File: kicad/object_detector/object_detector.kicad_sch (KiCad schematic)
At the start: 0 parts

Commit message: put my sutff on kicad schematic
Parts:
- added C1: 220u, Capacitor_SMD:CP_Elec_8x10, symbol Device:C_Polarized
- added C2: 100n, Capacitor_SMD:C_1206_3216Metric_Pad1.33x1.80mm_HandSolder, symbol Device:C_Small
- added C3: 1u, Capacitor_THT:C_Rect_L7.0mm_W4.5mm_P5.00mm, symbol Device:C_Small
- added C4: 47n, Resistor_SMD:R_0805_2012Metric_Pad1.20x1.40mm_HandSolder, symbol Device:C_Small
- added Display: Conn_01x04, Connector_JST:JST_PH_B4B-PH-K_1x04_P2.00mm_Vertical, symbol Connector_Generic:Conn_01x04
- added R1: 100R, Resistor_SMD:R_1206_3216Metric_Pad1.30x1.75mm_HandSolder, symbol Device:R_Small_US
- added Speaker: Conn_01x02, Connector_JST:JST_PH_B2B-PH-K_1x02_P2.00mm_Vertical, symbol Connector_Generic:Conn_01x02
- added TP1: DAC_signal, symbol Connector:TestPoint_Alt
- added TP2: Spk_signal, symbol Connector:TestPoint_Alt
- added TP3: SCL, symbol Connector:TestPoint_Alt
- added TP4: SDA, symbol Connector:TestPoint_Alt
- added U1: LM386, Package_SO:SOIC-8-1EP_3.9x4.9mm_P1.27mm_EP2.29x3mm, symbol Amplifier_Audio:LM386
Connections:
- new net: C1.1, C3.1, R1.2
- new net: C1.2, Speaker.1 (Pin_1), TP2.1
- new net: C2.1, TP1.1
- new net: C2.2, U1.3 (+)
- new net: C4.2, U1.7 (BYPASS)
- new net: R1.1, U1.5
- new net 5V: Display.1 (Pin_1), U1.6 (V+)
- new net GND: C3.2, C4.1, Display.2 (Pin_2), Speaker.2 (Pin_2), U1.2 (-), U1.4 (GND)
- new net SCL: Display.3 (Pin_3), TP3.1
- new net SDA: Display.4 (Pin_4), TP4.1

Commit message: kicad layout for ramus stuff
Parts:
- added BUTTONS1, SENSOR1: Conn_01x05, Connector_JST:JST_PH_B5B-PH-K_1x05_P2.00mm_Vertical, symbol Connector_Generic:Conn_01x05
- added C5: 100n, Capacitor_SMD:C_1206_3216Metric_Pad1.33x1.80mm_HandSolder, symbol Device:C_Small
- added µC1: ~, RF_Module:ESP32-C3-DevKitM-1, symbol custom_ece342:ESP32_WROOM
- TP1, TP2: footprint (none) -> TestPoint:TestPoint_2Pads_Pitch5.08mm_Drill1.3mm
- TP3, TP4: footprint (none) -> Connector_PinHeader_2.54mm:PinHeader_1x01_P2.54mm_Vertical
- renumbered Display to Display1, Speaker to Speaker1
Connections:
- net 5V: now also C5.2, µC1. (3.3V)
- net GND: now also BUTTONS1.5 (Pin_5), C5.1, SENSOR1.5 (Pin_5), µC1. (3.3V)
- net SCL: now also µC1. (3.3V)
- net SDA: now also µC1. (3.3V)
- net DAC: now reaches C2.1, TP1.1
- net DAC: now also µC1. (3.3V)
- new net BRIGHTNESS: BUTTONS1.2 (Pin_2)
- new net RESET: BUTTONS1.1 (Pin_1), µC1. (3.3V)
- new net TIME_DEC: BUTTONS1.4 (Pin_4)
- new net TIME_INC: BUTTONS1.3 (Pin_3)
- new net WEIGH_1: SENSOR1.1 (Pin_1)
- new net WEIGH_2: SENSOR1.2 (Pin_2)
- new net WEIGH_3: SENSOR1.3 (Pin_3)
- new net WEIGH_4: SENSOR1.4 (Pin_4)
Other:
- note added: "2/20/2026"
- note added: "ECE 342 – Group 01 Nick Gerbavac John Ramus Arthur Roth"
- note added: "Object Detector"

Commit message: updated PCB schematic
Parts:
- removed µC1: ~, RF_Module:ESP32-C3-DevKitM-1, symbol custom_ece342:ESP32_WROOM
- added C6, C7: 10uF, Capacitor_SMD:C_1206_3216Metric, symbol Device:C
- added D1: B220, Diode_SMD:D_SMA, symbol Device:D_Schottky
- added D2: LED, LED_SMD:LED_0603_1608Metric, symbol Device:LED
- added H1, H2, H3, H4: MountingHole, MountingHole:MountingHole_2.2mm_M2, symbol Mechanical:MountingHole
- added J1: Terminal In, TerminalBlock_TE-Connectivity:TerminalBlock_TE_282834-2_1x02_P2.54mm_Horizontal, symbol Connector:Screw_Terminal_01x02
- added R2: 560, Resistor_SMD:R_0805_2012Metric, symbol Device:R
- added U2: ESP32_DevKitC, ESP32:ESP32_DevKitC_38pin_socket, symbol ESP32:ESP32_DevKitC
- added U3: NCP1117-5.0_SOT223, Package_TO_SOT_SMD:SOT-223-3_TabPin2, symbol ncp1117-5.0_sot223:NCP1117-5.0_SOT223
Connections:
- net 5V: now also C7.1, U2.19 (5V_in), U3.2 (VO)
- net BRIGHTNESS: now also U2.31 (IO_19)
- net DAC: now also U2.9 (IO_25)
- net GND: now also C6.2, C7.2, D2.1 (K), J1.1 (Pin_1), U2.14 (GND), U2.32 (GND), U2.38 (GND), U3.1 (GND)
- net RESET: now also U2.2 (EN)
- net SCL: now also U2.36 (IO_22)
- net SDA: now also U2.33 (IO_21)
- net TIME_DEC: now also U2.28 (IO_17)
- net TIME_INC: now also U2.30 (IO_18)
- net WEIGH_1: now also U2.10 (IO_26)
- net WEIGH_2: now also U2.11 (IO_27)
- net WEIGH_3: now also U2.7 (IO_32)
- net WEIGH_4: now also U2.8 (IO_33)
- new net: C6.1, D1.1 (K), R2.1, U3.3 (VI)
- new net: D2.2 (A), R2.2
- new net: D1.2 (A), J1.2 (Pin_2)
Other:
- note added: "5V Power Supply"
- note added: "Alarm and Display"
- note added: "ECE 342 – Group 01 Nicholas Gerbavac John Ramus Arthur Roth"
- note added: "ESP32 DevKitC Module"
- note added: "M2 Screws"
- note added: "Mounting Holes"
- note added: "UI Buttons and Object Sensor output"
- note removed: "ECE 342 – Group 01 Nick Gerbavac John Ramus Arthur Roth"
- moved on the sheet: BUTTONS1, C1, C2, C3, C4, C5, Display1, R1, SENSOR1, Speaker1, TP1, TP2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

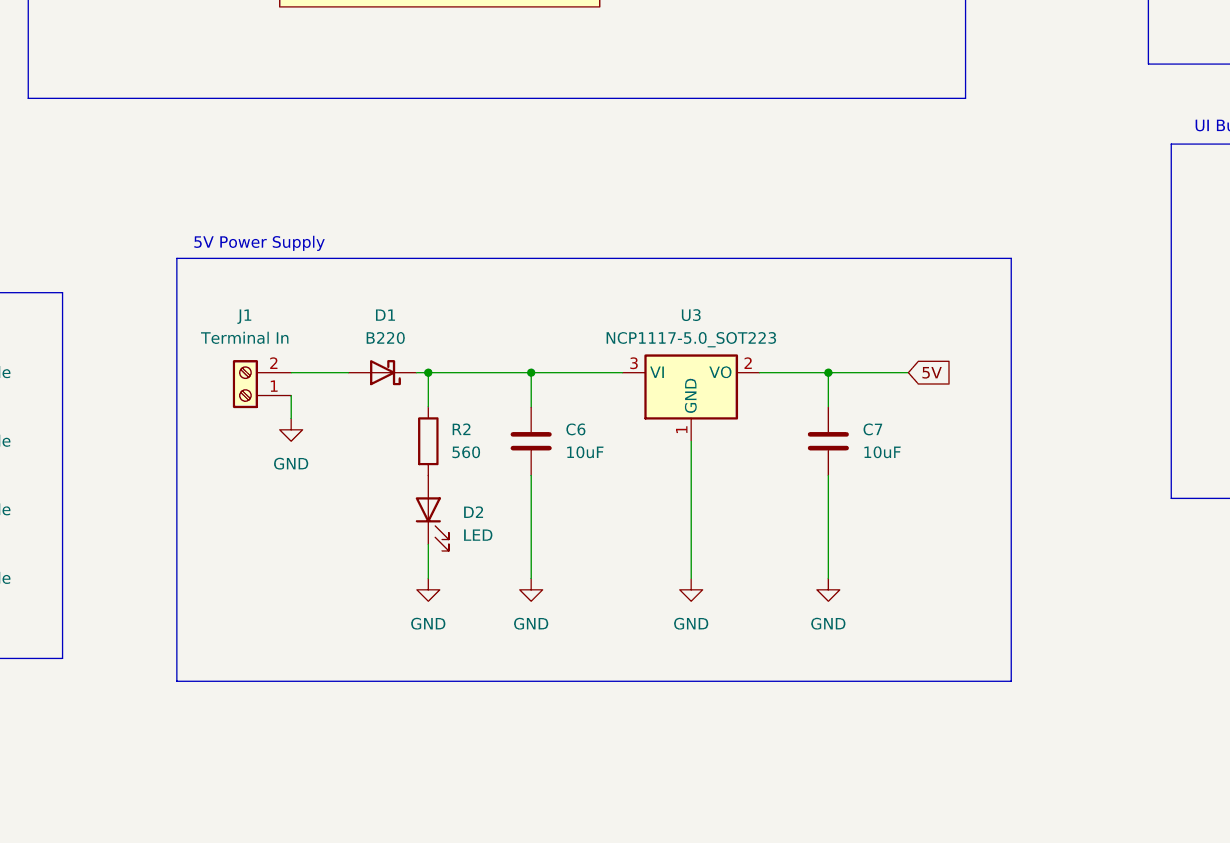
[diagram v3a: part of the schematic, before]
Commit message: changed LDO connector input
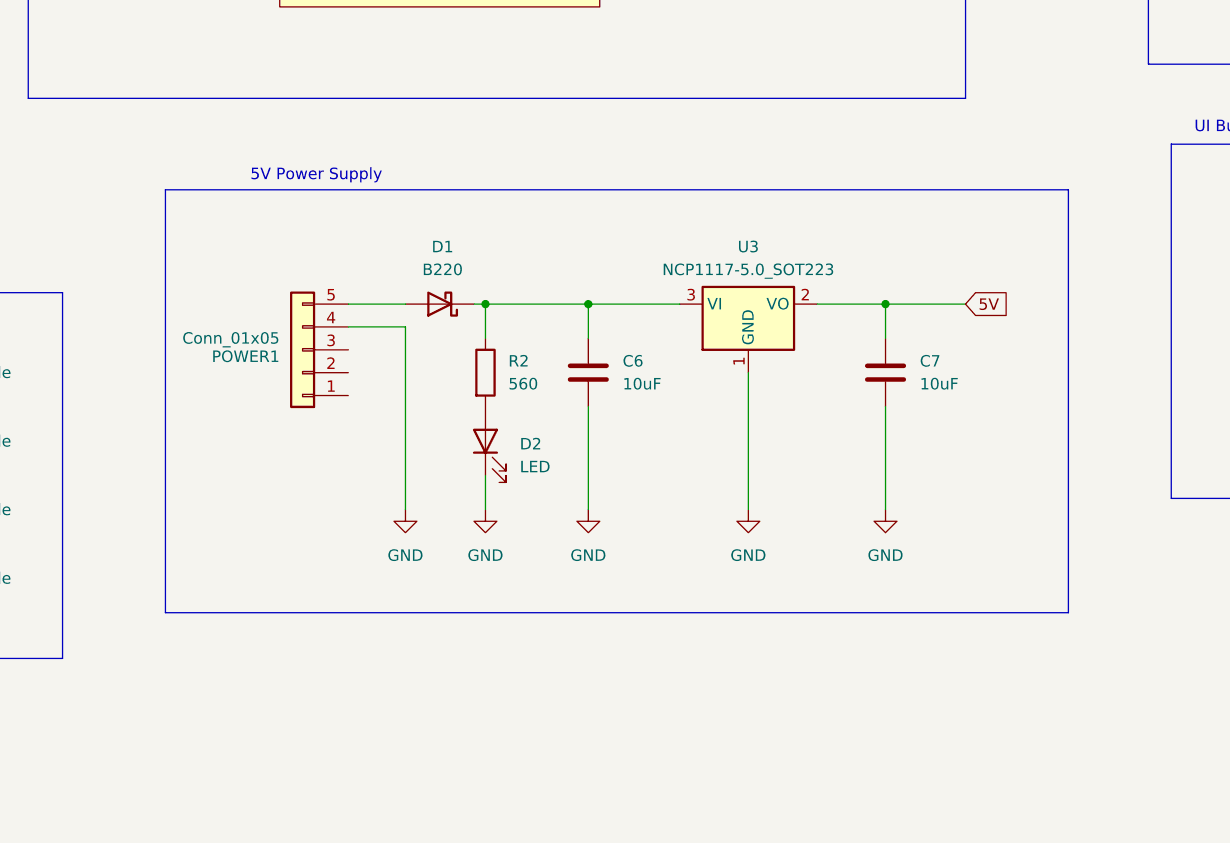
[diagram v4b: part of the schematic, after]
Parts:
- removed J1: Terminal In, TerminalBlock_TE-Connectivity:TerminalBlock_TE_282834-2_1x02_P2.54mm_Horizontal, symbol Connector:Screw_Terminal_01x02
- added POWER1: Conn_01x05, Connector_JST:JST_PH_B5B-PH-K_1x05_P2.00mm_Vertical, symbol Connector_Generic:Conn_01x05
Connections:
- net GND: now also POWER1.4 (Pin_4)
- net at D1.2 (A): now also POWER1.5 (Pin_5)
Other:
- moved on the sheet: C6, C7, D1, D2, R2, U3

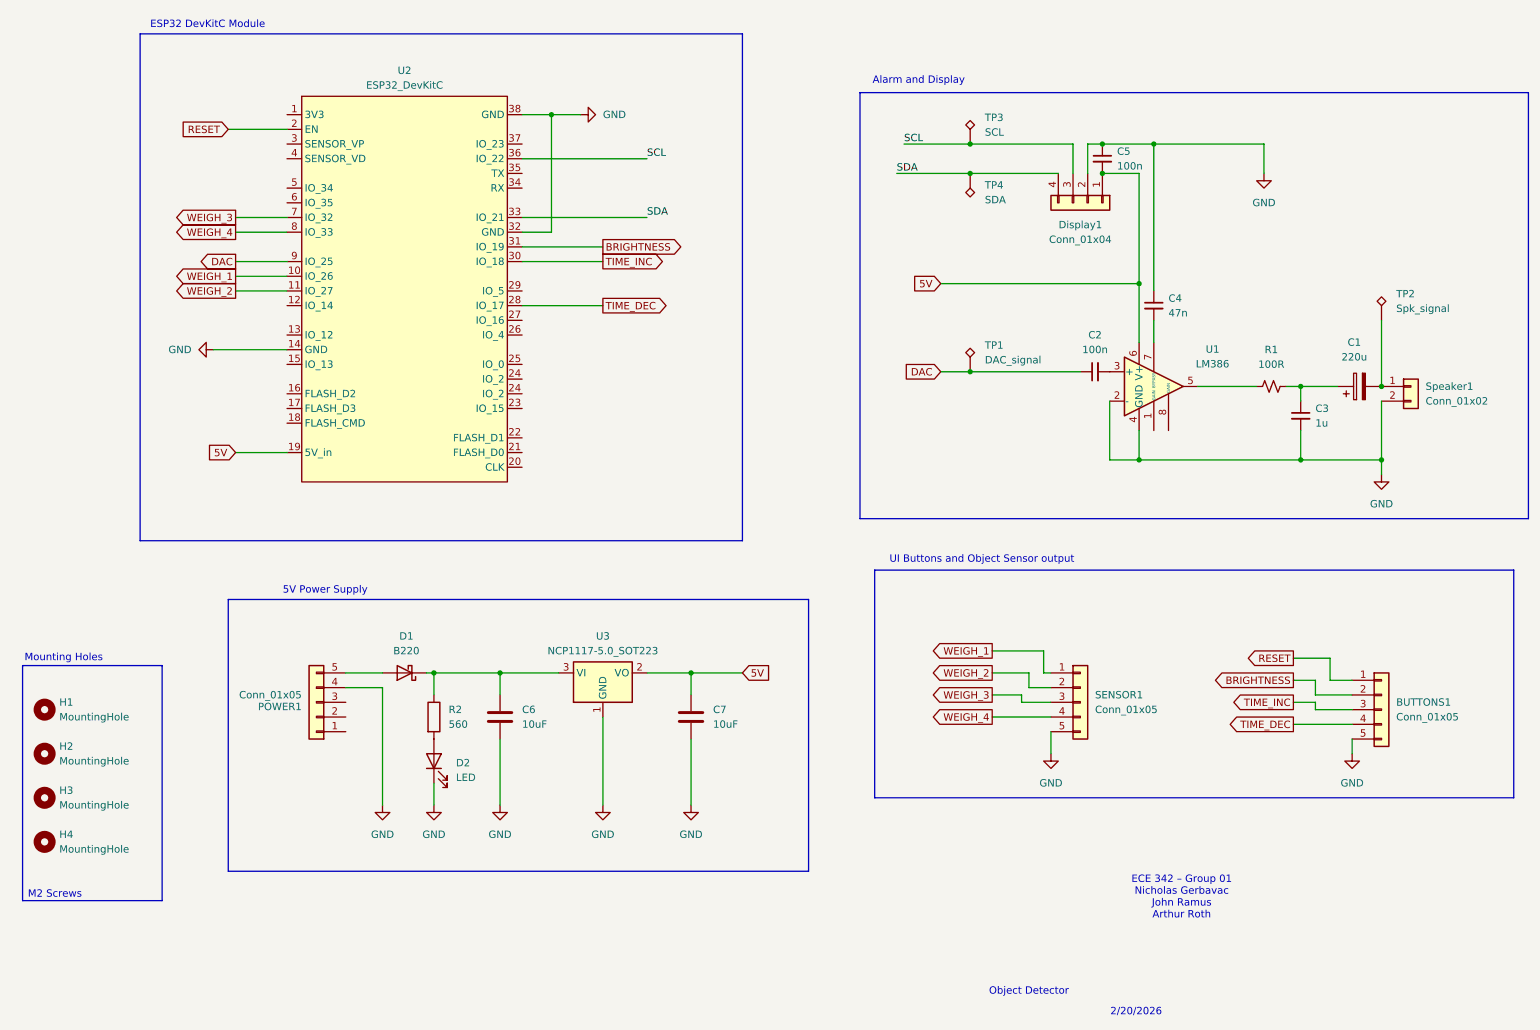
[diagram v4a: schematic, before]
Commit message: preliminary layout
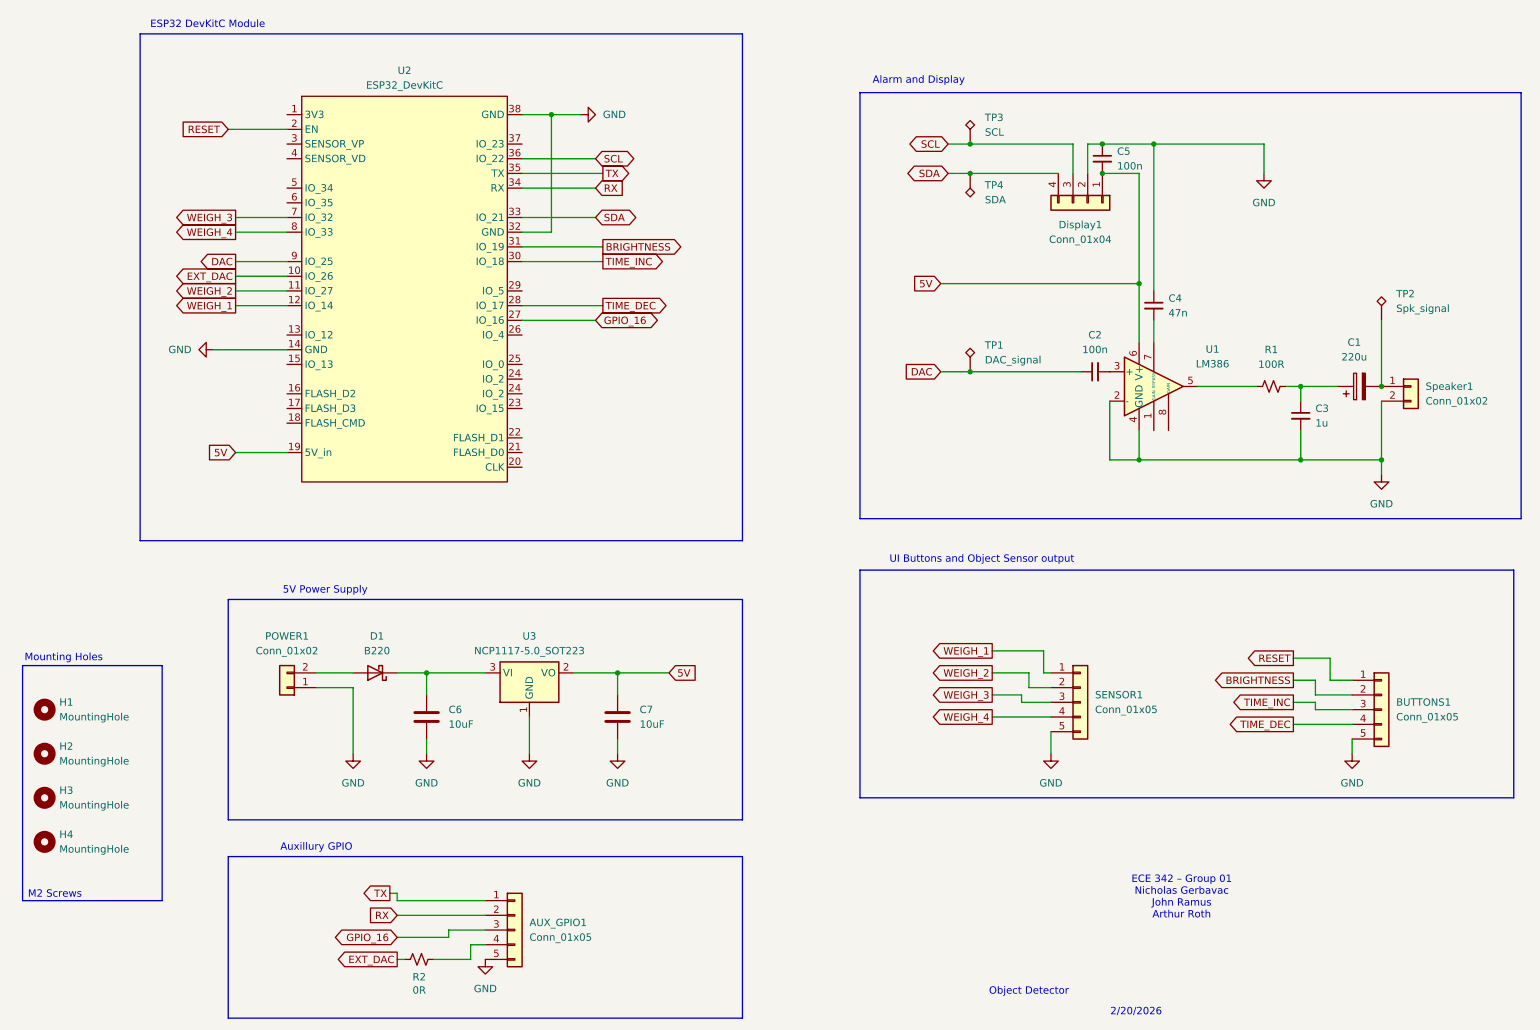
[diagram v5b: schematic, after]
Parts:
- removed D2: LED, LED_SMD:LED_0603_1608Metric, symbol Device:LED
- removed POWER1: Conn_01x05, Connector_JST:JST_PH_B5B-PH-K_1x05_P2.00mm_Vertical, symbol Connector_Generic:Conn_01x05
- removed R2: 560, Resistor_SMD:R_0805_2012Metric, symbol Device:R
- added AUX_GPIO1: Conn_01x05, Connector_JST:JST_PH_B5B-PH-K_1x05_P2.00mm_Vertical, symbol Connector_Generic:Conn_01x05
- added POWER1: Conn_01x02, Connector_JST:JST_PH_B2B-PH-K_1x02_P2.00mm_Vertical, symbol Connector_Generic:Conn_01x02
- added R2: 0R, Resistor_SMD:R_1206_3216Metric_Pad1.30x1.75mm_HandSolder, symbol Device:R_Small_US
- U2: footprint ESP32:ESP32_DevKitC_38pin_socket -> PCM_Espressif:ESP32-DevKitC
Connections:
- net GND: now also AUX_GPIO1.5 (Pin_5), POWER1.1 (Pin_1)
- net WEIGH_1: now also U2.12 (IO_14); no longer U2.10 (IO_26)
- net GPIO_16: now reaches U2.27 (IO_16)
- net GPIO_16: now also AUX_GPIO1.3 (Pin_3)
- net RX: now reaches U2.34 (RX)
- net RX: now also AUX_GPIO1.2 (Pin_2)
- net TX: now reaches U2.35 (TX)
- net TX: now also AUX_GPIO1.1 (Pin_1)
- net at D1.2 (A): now also POWER1.2 (Pin_2)
- new net: AUX_GPIO1.4 (Pin_4), R2.2
- new net EXT_DAC: R2.1, U2.10 (IO_26)
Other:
- note added: "Auxillury GPIO"
- moved on the sheet: C6, C7, D1, U3

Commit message: board revision friday
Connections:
- net GND: now also Speaker1.1 (Pin_1); no longer Speaker1.2 (Pin_2)
- net at C1.2, TP2.1: now also Speaker1.2 (Pin_2); no longer Speaker1.1 (Pin_1)
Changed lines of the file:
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@@
 	)
 	(symbol
+		(lib_name "Conn_01x02_1")
 		(lib_id "Connector_Generic:Conn_01x02")
 		(at 260.35 85.09 0)
